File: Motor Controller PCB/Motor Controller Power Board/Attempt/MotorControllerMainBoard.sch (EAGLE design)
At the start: 47 parts

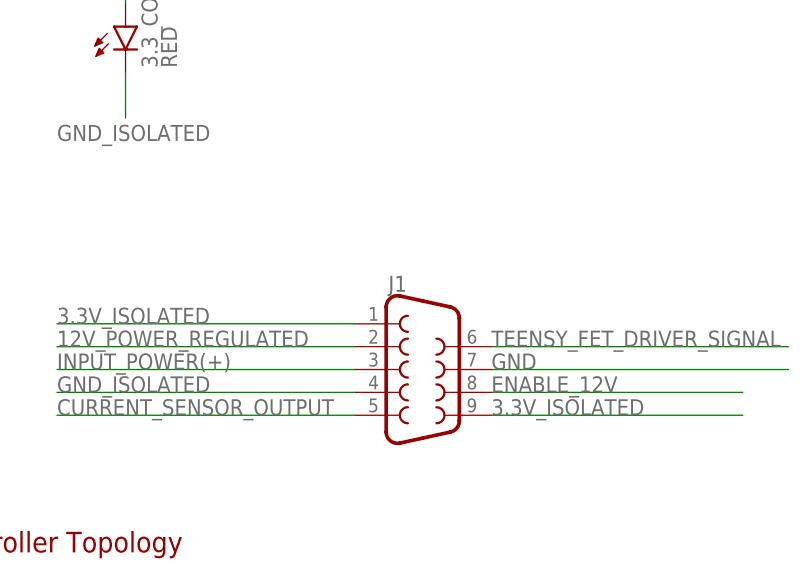
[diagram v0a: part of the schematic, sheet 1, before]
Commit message: Doing a new layout
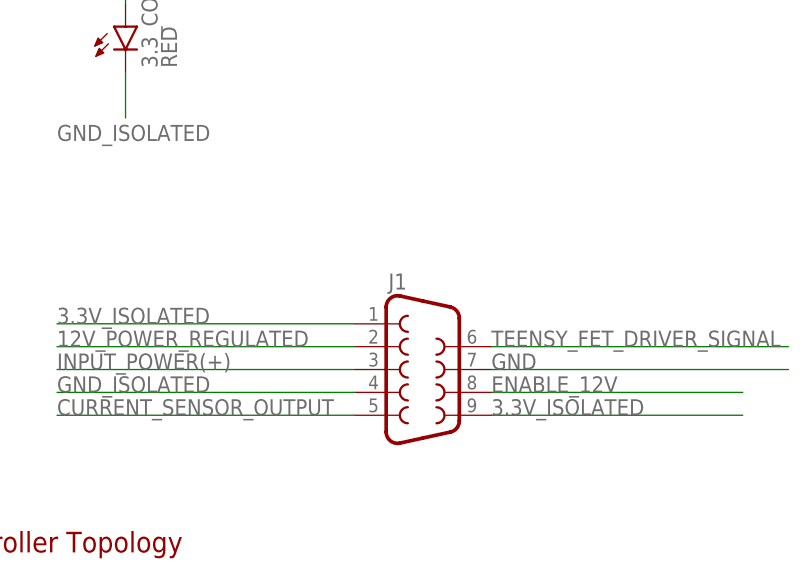
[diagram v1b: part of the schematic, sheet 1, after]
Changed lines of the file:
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@@
 <part name="GND5" library="supply1" library_urn="urn:adsk.eagle:library:371" deviceset="GND" device=""/>
 <part name="GND6" library="supply1" library_urn="urn:adsk.eagle:library:371" deviceset="GND" device=""/>
-<part name="J1" library="SparkFun-Connectors" library_urn="urn:adsk.eagle:library:513" deviceset="DB9" device="FEMALE" package3d_urn="urn:adsk.eagle:package:38025/1"/>
+<part name="J1" library="SparkFun-Connectors" deviceset="DB9" device="FEMALE"/>
 <part name="U$7" library="MotorControllerEagleLibrary" deviceset="SMBJ15CD" device=""/>
 <part name="U$20" library="MotorControllerEagleLibrary" deviceset="SMBJ15CD" device=""/>

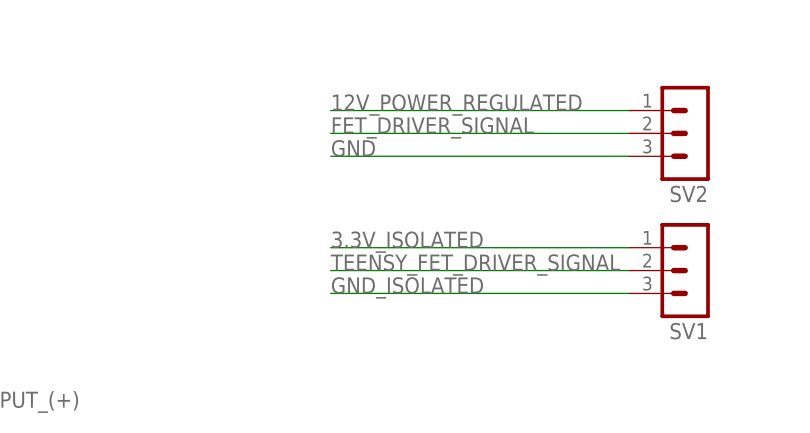
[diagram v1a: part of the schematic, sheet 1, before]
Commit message: Started routing new layout
think this is the one bois
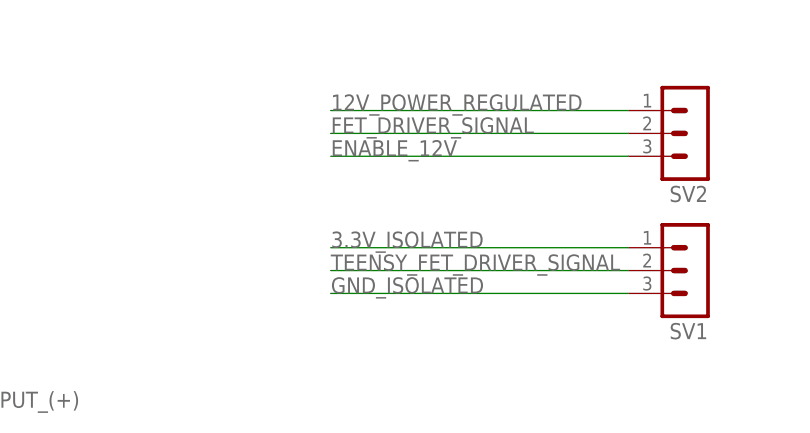
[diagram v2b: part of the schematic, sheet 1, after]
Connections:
- net ENABLE_12V: now also SV2.3
- net GND: no longer SV2.3
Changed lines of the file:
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@@
 <?xml version="1.0" encoding="utf-8"?>
 <!DOCTYPE eagle SYSTEM "eagle.dtd">
-<eagle version="8.6.0">
+<eagle version="8.7.0">
 <drawing>
 <settings>
@@
 <pinref part="J1" gate="G$1" pin="7"/>
 </segment>
-<segment>
-<wire x1="259.08" y1="185.42" x2="226.06" y2="185.42" width="0.1524" layer="91"/>
-<label x="226.06" y="185.42" size="1.778" layer="95"/>
-<pinref part="SV2" gate="G$1" pin="3"/>
-</segment>
 </net>
 <net name="FET_DRIVER_SIGNAL" class="0">
@@
 <label x="246.38" y="48.26" size="1.778" layer="95"/>
 </segment>
-</net>
+<segment>
+<wire x1="259.08" y1="185.42" x2="226.06" y2="185.42" width="0.1524" layer="91"/>
+<label x="226.06" y="185.42" size="1.778" layer="95"/>
+<pinref part="SV2" gate="G$1" pin="3"/>
+</segment>
+</net>
